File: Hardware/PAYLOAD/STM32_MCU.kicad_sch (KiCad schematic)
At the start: 16 parts

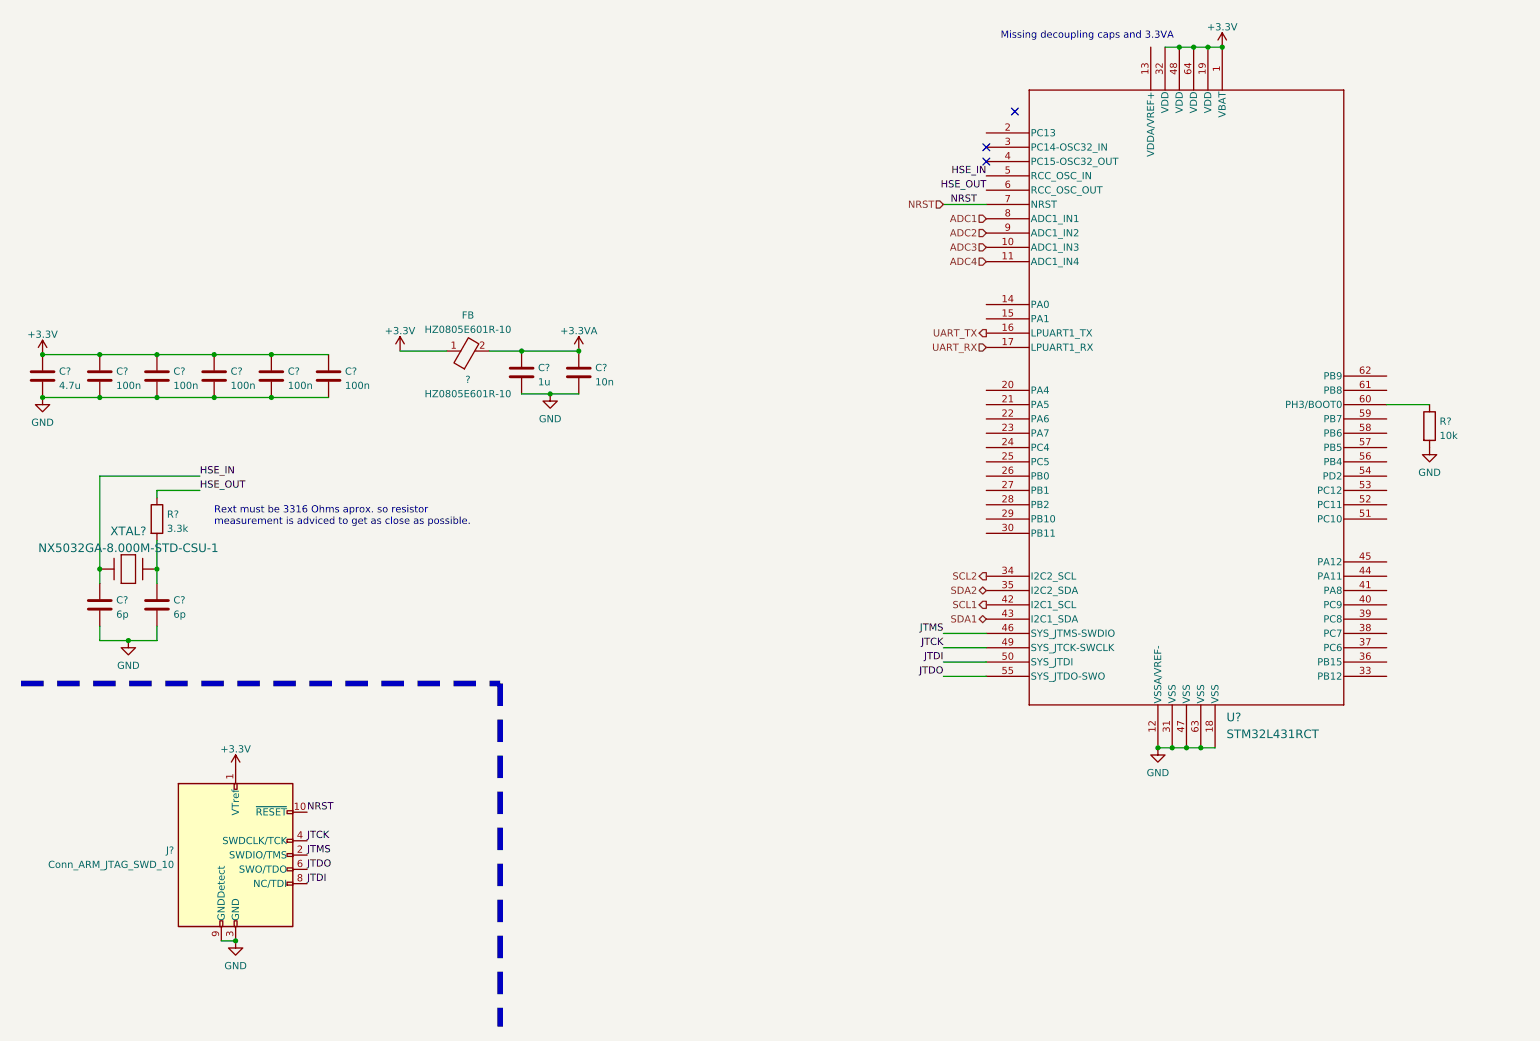
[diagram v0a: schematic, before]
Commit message: Created Payload Board
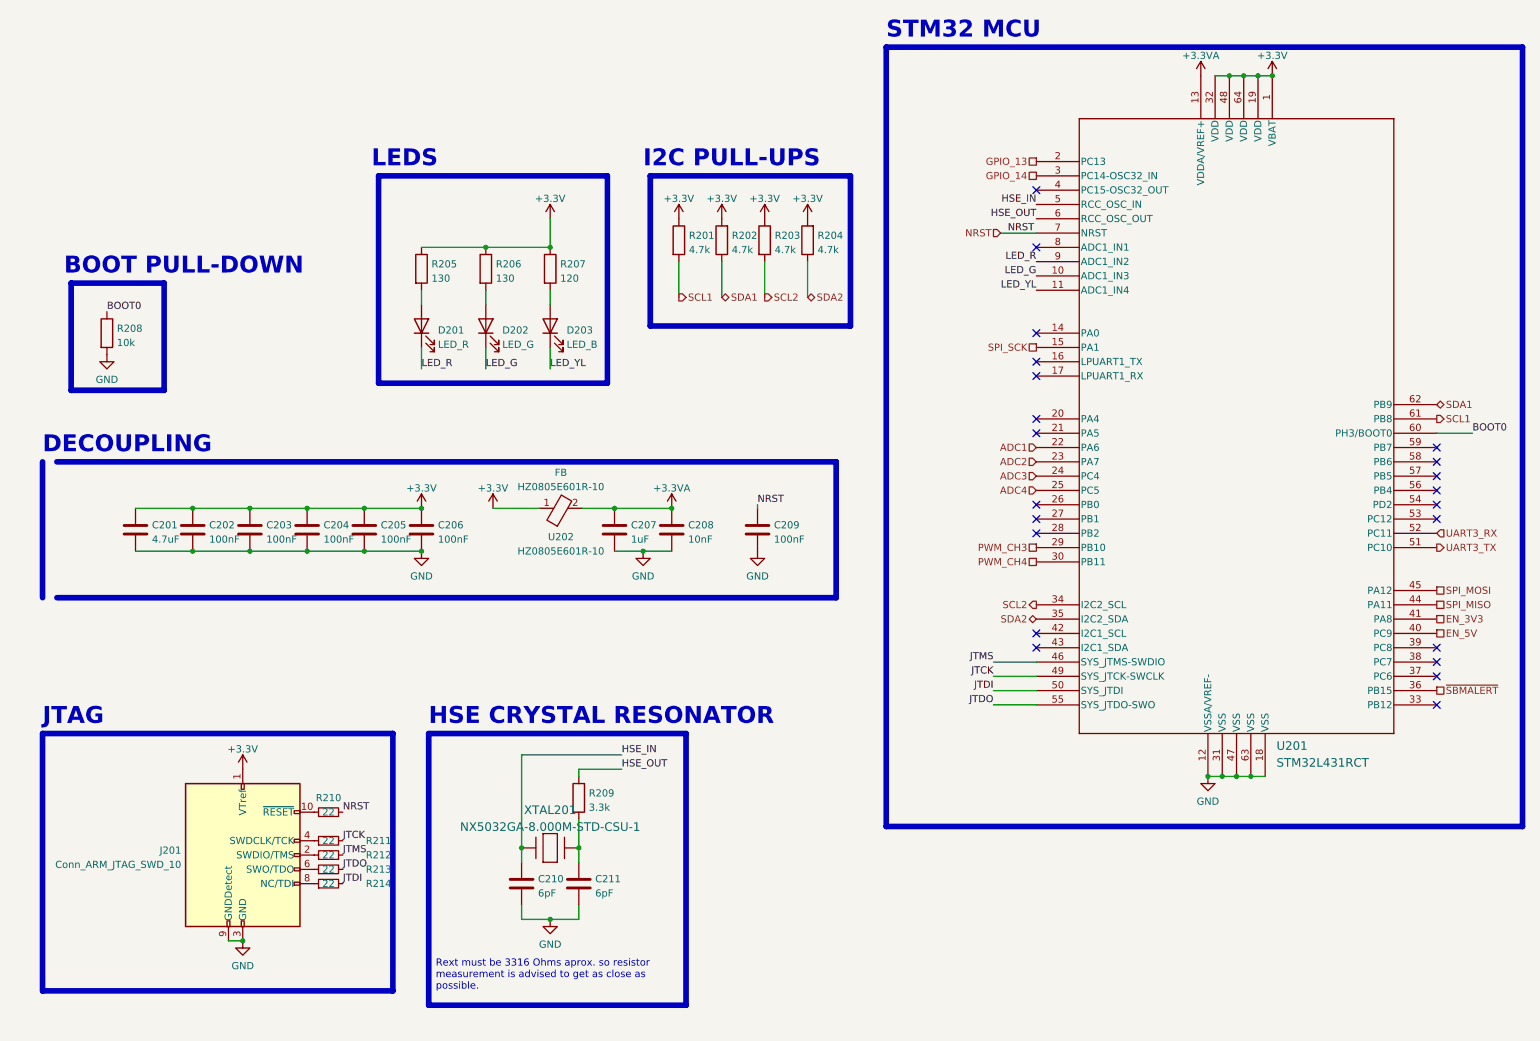
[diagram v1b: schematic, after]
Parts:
- removed R?: 10k, symbol Device:R
- added C209: 100nF, Capacitor_SMD:C_0603_1608Metric_Pad1.08x0.95mm_HandSolder, symbol Device:C
- added D201: LED_R, LED_SMD:LED_0603_1608Metric, symbol Device:LED
- added D202: LED_G, LED_SMD:LED_0603_1608Metric, symbol Device:LED
- added D203: LED_B, LED_SMD:LED_0603_1608Metric, symbol Device:LED
- added R201, R202, R203, R204: 4.7k, Resistor_SMD:R_0603_1608Metric_Pad0.98x0.95mm_HandSolder, symbol Device:R
- added R205, R206: 130, Resistor_SMD:R_0603_1608Metric_Pad0.98x0.95mm_HandSolder, symbol Device:R
- added R207: 120, Resistor_SMD:R_0603_1608Metric_Pad0.98x0.95mm_HandSolder, symbol Device:R
- added R208: 10k, Resistor_SMD:R_0603_1608Metric_Pad0.98x0.95mm_HandSolder, symbol Device:R
- added R210, R211, R212, R213, R214: 22, Resistor_SMD:R_0603_1608Metric_Pad0.98x0.95mm_HandSolder, symbol Device:R_Small
- C201: renamed from C?; value 4.7u -> 4.7uF; footprint (none) -> Capacitor_SMD:C_0603_1608Metric_Pad1.08x0.95mm_HandSolder
- C202, C203, C204, C205, C206: renamed from C?; value 100n -> 100nF; footprint (none) -> Capacitor_SMD:C_0603_1608Metric_Pad1.08x0.95mm_HandSolder
- C207: renamed from C?; value 1u -> 1uF; footprint (none) -> Capacitor_SMD:C_0603_1608Metric_Pad1.08x0.95mm_HandSolder
- C208: renamed from C?; value 10n -> 10nF; footprint (none) -> Capacitor_SMD:C_0603_1608Metric_Pad1.08x0.95mm_HandSolder
- C210, C211: renamed from C?; value 6p -> 6pF; footprint (none) -> Capacitor_SMD:C_0603_1608Metric_Pad1.08x0.95mm_HandSolder
- J201: renamed from J?; footprint (none) -> digikey-footprints:PinHeader_2x5_P1.27mm_Drill.7mm
- R209: renamed from R?; footprint (none) -> Resistor_SMD:R_0603_1608Metric_Pad0.98x0.95mm_HandSolder
- U201: renamed from U?; footprint LQFP-64 -> STM32L431RCT:LQFP-64
- U202: renamed from ?; footprint (none) -> HZ0805E601R-10:BEADC2012X90N
- XTAL201: renamed from XTAL?; footprint XTAL_NX5032_NDK -> NX5032GA-8.000M:XTAL_NX5032_NDK
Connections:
- net +3.3V: now also R201.1, R202.2, R203.1, R204.2, R205.1, R206.1, R207.1
- net +3.3VA: now also U201.13 (VDDA/VREF+)
- net ADC1: now also U201.22 (PA6); no longer U201.8 (ADC1_IN1)
- net ADC2: now also U201.23 (PA7); no longer U201.9 (ADC1_IN2)
- net ADC3: now also U201.24 (PC4); no longer U201.10 (ADC1_IN3)
- net ADC4: now also U201.25 (PC5); no longer U201.11 (ADC1_IN4)
- net GND: now also C209.2, R208.2
- net JTCK: now also R211.2; no longer J201.4 (SWDCLK/TCK)
- net JTDI: now also R214.2; no longer J201.8 (NC/TDI)
- net JTDO: now also R213.2; no longer J201.6 (SWO/TDO)
- net JTMS: now also R212.2; no longer J201.2 (SWDIO/TMS)
- net NRST: now also C209.1, R210.2; no longer J201.10 (~{RESET})
- net SCL1: now also U201.61 (PB8), R201.2; no longer U201.42 (I2C1_SCL)
- net SCL2: now also R203.2
- net SDA1: now also U201.62 (PB9), R202.1; no longer U201.43 (I2C1_SDA)
- net SDA2: now also R204.1
- net SPI_SCK: now reaches U201.15 (PA1)
- net GPIO_13: now reaches U201.2 (PC13)
- net PWM_CH3: now reaches U201.29 (PB10)
- net GPIO_14: now reaches U201.3 (PC14-OSC32_IN)
- net PWM_CH4: now reaches U201.30 (PB11)
- net ~{SBMALERT}: now reaches U201.36 (PB15)
- net EN_5V: now reaches U201.40 (PC9)
- net EN_3V3: now reaches U201.41 (PA8)
- net SPI_MISO: now reaches U201.44 (PA11)
- net SPI_MOSI: now reaches U201.45 (PA12)
- net UART3_TX: now reaches U201.51 (PC10)
- net UART3_RX: now reaches U201.52 (PC11)
- net BOOT0: now reaches U201.60 (PH3/BOOT0)
- net BOOT0: now also R208.1
- net UART_RX: no longer names the net of U201.17 (LPUART1_RX)
- net UART_TX: no longer names the net of U201.16 (LPUART1_TX)
- new net: J201.10 (~{RESET}), R210.1
- new net: J201.2 (SWDIO/TMS), R212.1
- new net: J201.4 (SWDCLK/TCK), R211.1
- new net: J201.6 (SWO/TDO), R213.1
- new net: J201.8 (NC/TDI), R214.1
- new net: D202.2 (A), R206.2
- new net: D203.2 (A), R207.2
- new net: D201.2 (A), R205.2
- new net LED_G: D202.1 (K), U201.10 (ADC1_IN3)
- new net LED_R: D201.1 (K), U201.9 (ADC1_IN2)
- new net LED_YL: D203.1 (K), U201.11 (ADC1_IN4)
- no-connect marks 3 -> 22
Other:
- note added: "BOOT PULL-DOWN"
- note added: "DECOUPLING"
- note added: "HSE CRYSTAL RESONATOR"
- note added: "I2C PULL-UPS"
- note added: "JTAG"
- note added: "LEDS"
- note added: "Rext must be 3316 Ohms aprox. so resistor measurement is advised to get as close as possible."
- note added: "STM32 MCU"
- note removed: "Missing decoupling caps and 3.3VA"
- note removed: "Rext must be 3316 Ohms aprox. so resistor measurement is adviced to get as close as possible."
- moved on the sheet: C201, C202, C203, C204, C205, C206, C207, C208, C210, C211, J201, R209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

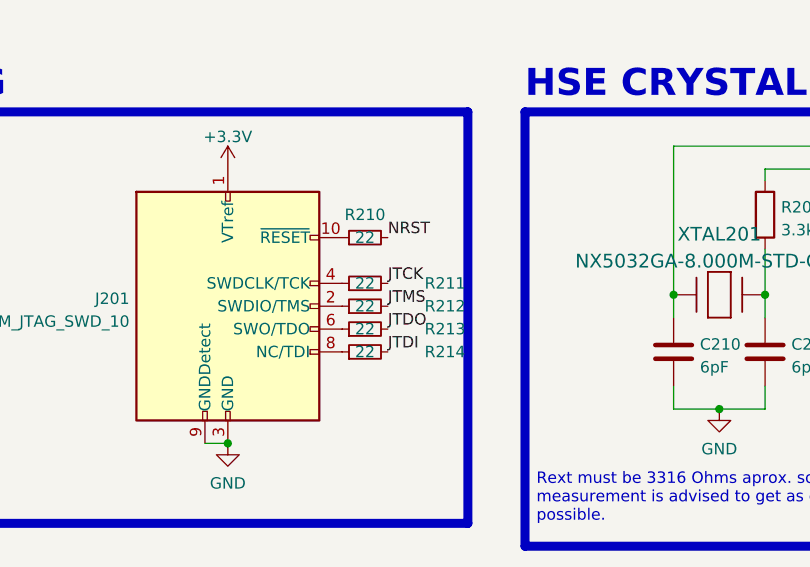
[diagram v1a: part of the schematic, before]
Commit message: Updated to KiCAD 7.0
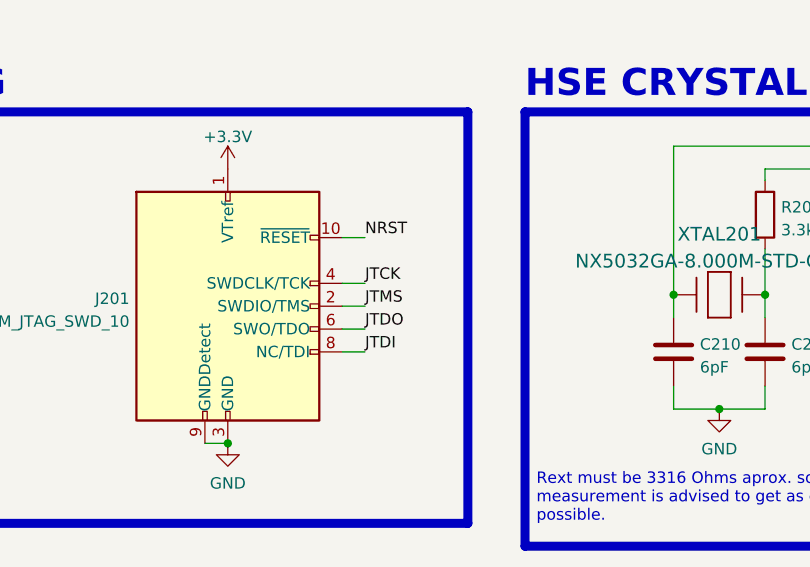
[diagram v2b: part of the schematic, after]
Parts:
- removed R210, R211, R212, R213, R214: 22, Resistor_SMD:R_0603_1608Metric_Pad0.98x0.95mm_HandSolder, symbol Device:R_Small
- J201: footprint digikey-footprints:PinHeader_2x5_P1.27mm_Drill.7mm -> Connector_PinHeader_2.00mm:PinHeader_2x05_P2.00mm_Vertical
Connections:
- net JTCK: now also J201.4 (SWDCLK/TCK)
- net JTDI: now also J201.8 (NC/TDI)
- net JTDO: now also J201.6 (SWO/TDO)
- net JTMS: now also J201.2 (SWDIO/TMS)
- net NRST: now also J201.10 (~{RESET})
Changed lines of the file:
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@@
     (stroke (width 0) (type default) (color 0 0 0 0))
   )
+  (wire (pts (xy 67.31 170.18) (xy 64.77 170.18))
+    (stroke (width 0) (type default) (color 0 0 0 0))
+  )
   (wire (pts (xy 185.42 140.97) (xy 193.04 140.97))
     (stroke (width 0) (type default) (color 0 0 0 0))
@@
     (stroke (width 1) (type default) (color 0 0 0 0))
   )
+  (wire (pts (xy 67.31 172.72) (xy 64.77 172.72))
+    (stroke (width 0) (type default) (color 0 0 0 0))
+  )
   (polyline (pts (xy 21.59 66.04) (xy 38.1 66.04))
     (stroke (width 1) (type default) (color 0 0 0 0))
@@
     (stroke (width 1) (type default) (color 0 0 0 0))
   )
+  (wire (pts (xy 67.31 167.64) (xy 64.77 167.64))
+    (stroke (width 0) (type default) (color 0 0 0 0))
+  )
   (polyline (pts (xy 124.46 46.99) (xy 160.02 46.99))
     (stroke (width 1) (type default) (color 0 0 0 0))
@@
     (stroke (width 0) (type default) (color 0 0 0 0))
   )
+  (wire (pts (xy 67.31 165.1) (xy 64.77 165.1))
+    (stroke (width 0) (type default) (color 0 0 0 0))
+  )
   (wire (pts (xy 143.51 106.045) (xy 143.51 105.41))
     (stroke (width 0) (type default) (color 0 0 0 0))
@@
     (stroke (width 0) (type default) (color 0 0 0 0))
   )
+  (wire (pts (xy 64.77 160.02) (xy 67.31 160.02))
+    (stroke (width 0) (type default) (color 0 0 0 0))
+  )
   (polyline (pts (xy 279.4 162.56) (xy 166.37 162.56))
     (stroke (width 1) (type default) (color 0 0 0 0))
@@
     (effects (font (size 1.27 1.27)) (justify left bottom))
   )
-  (label "NRST" (at 69.85 160.02 0)
+  (label "NRST" (at 67.31 160.02 0)
     (effects (font (size 1.27 1.27)) (justify left bottom))
   )
-  (label "JTDI" (at 69.85 172.72 0)
+  (label "JTDI" (at 67.31 172.72 0)
     (effects (font (size 1.27 1.27)) (justify left bottom))
   )
-  (label "JTMS" (at 69.85 167.64 0)
+  (label "JTMS" (at 67.31 167.64 0)
     (effects (font (size 1.27 1.27)) (justify left bottom))
   )
@@
     (effects (font (size 1.27 1.27)) (justify right bottom))
   )
-  (label "JTCK" (at 69.85 165.1 0)
+  (label "JTCK" (at 67.31 165.1 0)
     (effects (font (size 1.27 1.27)) (justify left bottom))
   )
@@
     (effects (font (size 1.27 1.27)) (justify right bottom))
   )
-  (label "JTDO" (at 69.85 170.18 0)
+  (label "JTDO" (at 67.31 170.18 0)
     (effects (font (size 1.27 1.27)) (justify left bottom))
   )
@@
       (effects (font (size 1.27 1.27)) (justify right))
     )
-    (property "Footprint" "digikey-footprints:PinHeader_2x5_P1.27mm_Drill.7mm" (id 2) (at 52.07 167.64 0)
+    (property "Footprint" "Connector_PinHeader_2.00mm:PinHeader_2x05_P2.00mm_Vertical" (id 2) (at 52.07 167.64 0)
       (effects (font (size 1.27 1.27)) hide)
     )
@@
     (pin "1")
   )
-  (symbol (lib_id "Device:R_Small") (at 67.31 167.64 90) (unit 1)
-    (in_bom yes) (on_board yes)
-    (property "Reference" "R212" (id 0) (at 76.2 167.64 90))
-    (property "Value" "22" (id 1) (at 67.31 167.64 90))
-    (property "Footprint" "Resistor_SMD:R_0603_1608Metric_Pad0.98x0.95mm_HandSolder" (id 2) (at 67.31 167.64 0)
-      (effects (font (size 1.27 1.27)) hide)
-    )
-    (property "Datasheet" "~" (id 3) (at 67.31 167.64 0)
-      (effects (font (size 1.27 1.27)) hide)
-    )
-    (pin "1")
-    (pin "2")
-  )
   (symbol (lib_id "STM32L431RCT:STM32L431RCT") (at 193.04 41.91 0) (unit 1)
     (in_bom yes) (on_board yes) (fields_autoplaced)
@@
     (pin "2")
   )
-  (symbol (lib_id "Device:R_Small") (at 67.31 165.1 90) (unit 1)
-    (in_bom yes) (on_board yes)
-    (property "Reference" "R211" (id 0) (at 76.2 165.1 90))
-    (property "Value" "22" (id 1) (at 67.31 165.1 90))
-    (property "Footprint" "Resistor_SMD:R_0603_1608Metric_Pad0.98x0.95mm_HandSolder" (id 2) (at 67.31 165.1 0)
-      (effects (font (size 1.27 1.27)) hide)
-    )
-    (property "Datasheet" "~" (id 3) (at 67.31 165.1 0)
-      (effects (font (size 1.27 1.27)) hide)
-    )
-    (pin "1")
-    (pin "2")
-  )
   (symbol (lib_id "Device:C") (at 53.34 109.855 0) (unit 1)
     (in_bom yes) (on_board yes) (fields_autoplaced)
@@
     (pin "1")
   )
-  (symbol (lib_id "Device:R_Small") (at 67.31 172.72 90) (unit 1)
-    (in_bom yes) (on_board yes)
-    (property "Reference" "R214" (id 0) (at 76.2 172.72 90))
-    (property "Value" "22" (id 1) (at 67.31 172.72 90))
-    (property "Footprint" "Resistor_SMD:R_0603_1608Metric_Pad0.98x0.95mm_HandSolder" (id 2) (at 67.31 172.72 0)
-      (effects (font (size 1.27 1.27)) hide)
-    )
-    (property "Datasheet" "~" (id 3) (at 67.31 172.72 0)
-      (effects (font (size 1.27 1.27)) hide)
-    )
-    (pin "1")
-    (pin "2")
-  )
   (symbol (lib_id "power:+3.3V") (at 129.54 54.61 0) (unit 1)
     (in_bom yes) (on_board yes) (fields_autoplaced)
@@
     (pin "2")
   )
-  (symbol (lib_id "Device:R_Small") (at 67.31 170.18 90) (unit 1)
-    (in_bom yes) (on_board yes)
-    (property "Reference" "R213" (id 0) (at 76.2 170.18 90))
-    (property "Value" "22" (id 1) (at 67.31 170.18 90))
-    (property "Footprint" "Resistor_SMD:R_0603_1608Metric_Pad0.98x0.95mm_HandSolder" (id 2) (at 67.31 170.18 0)
-      (effects (font (size 1.27 1.27)) hide)
-    )
-    (property "Datasheet" "~" (id 3) (at 67.31 170.18 0)
-      (effects (font (size 1.27 1.27)) hide)
-    )
-    (pin "1")
-    (pin "2")
-  )
   (symbol (lib_id "HZ0805E601R-10:HZ0805E601R-10") (at 108.585 106.045 0) (unit 1)
     (in_bom yes) (on_board yes)
@@
       (effects (font (size 1.27 1.27)) hide)
     )
-    (pin "1")
-    (pin "2")
-  )
-  (symbol (lib_id "Device:R_Small") (at 67.31 160.02 90) (unit 1)
-    (in_bom yes) (on_board yes)
-    (property "Reference" "R210" (id 0) (at 67.31 157.48 90))
-    (property "Value" "22" (id 1) (at 67.31 160.02 90))
-    (property "Footprint" "Resistor_SMD:R_0603_1608Metric_Pad0.98x0.95mm_HandSolder" (id 2) (at 67.31 160.02 0)
-      (effects (font (size 1.27 1.27)) hide)
-    )
-    (property "Datasheet" "~" (id 3) (at 67.31 160.02 0)
-      (effects (font (size 1.27 1.27)) hide)
-    )
